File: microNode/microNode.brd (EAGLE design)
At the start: 65 x 30 mm, 29 parts, among them U1 ATSAMD21G18A-AU, U2 TPL5111, U3 RFM95W-868S2, U4 MIC5504-3.3YM5-T5, U6 CLX6E-FKC-CH1M1D1BB7C3D3, U7 SIP32431DR3, U8 PCF2123, Y1 ABS07, Y2 ABS07

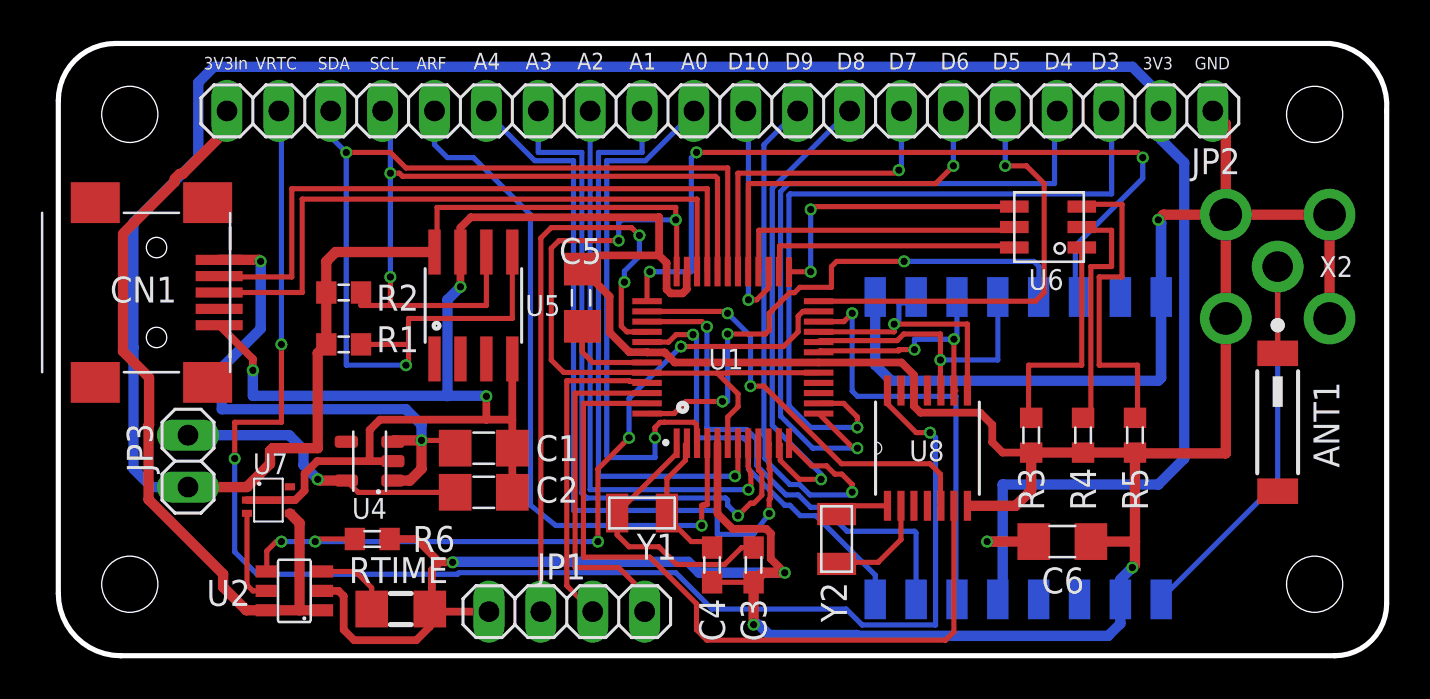
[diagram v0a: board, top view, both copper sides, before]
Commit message: Display connector/ RST button/ side led
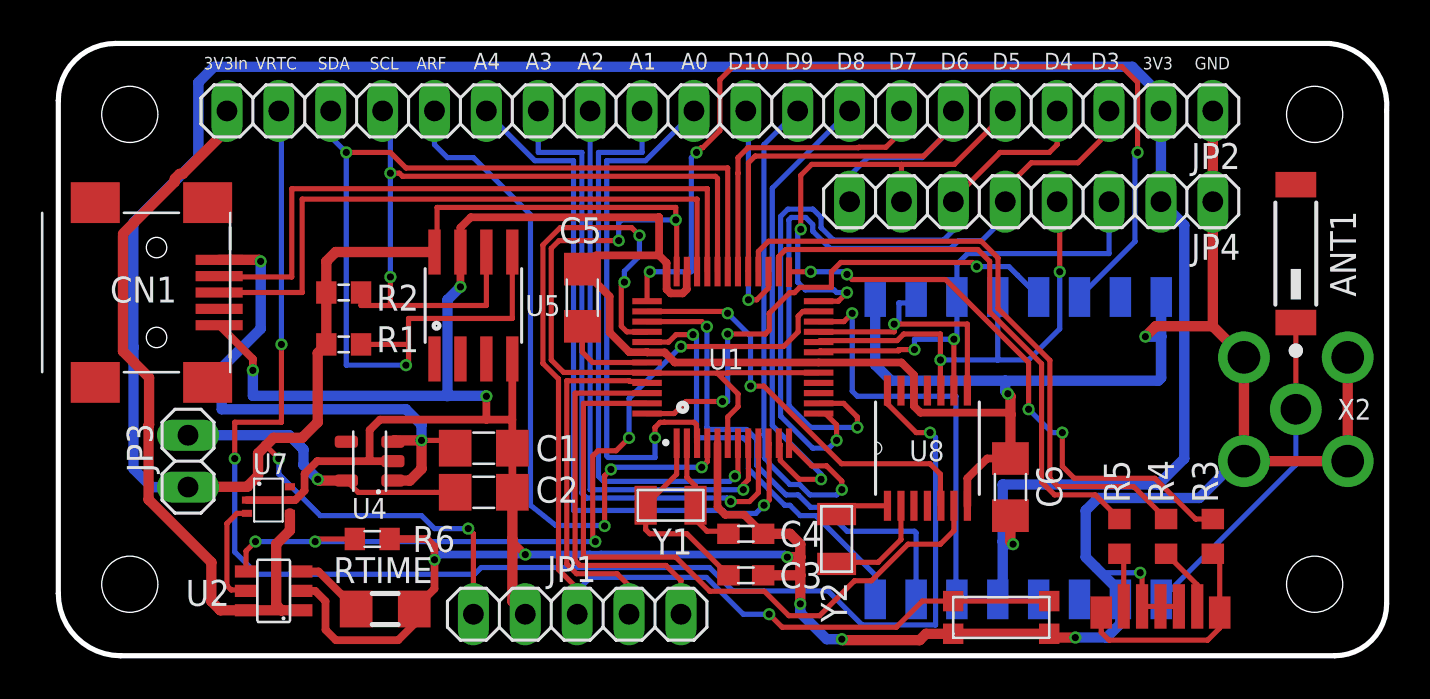
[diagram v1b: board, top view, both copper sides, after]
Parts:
- removed U6: CLX6E-FKC-CH1M1D1BB7C3D3, CLX6E-FKC:CLX6E-FKC-CH1M1D1BB7C3D3
- added JP4: (no value), pinhead:1X08
- added U$1: MSL0104RGB, MSL0104RGB:MSL0104RGB
- added U$2: KMR731NG, button:KMR731NG
- JP1: device pinhead:1X04 -> pinhead:1X05
- moved R3 10.2 mm to (104.8, 41.4)
- moved ANT1 8.30 mm to (108.8, 55.2), turned to 90 degrees
- moved X2 7.04 mm to (108.8, 47.6)
- moved R4 6.41 mm to (102.5, 41.4)
- moved R5 5.01 mm to (100.2, 41.4)
- moved C6 3.68 mm to (94.9, 43.8), turned to 90 degrees
- moved C4 2.25 mm to (81.9, 41.5), turned to 0 degrees
- moved Y1 1.45 mm to (78.2, 42.9)
- moved U2 1.02 mm to (58.8, 38.7)
- moved RTIME 0.76 mm to (64.3, 37.8)
- moved C3 0.64 mm to (81.9, 39.5), turned to 0 degrees
- moved JP1 0.52 mm to (73.7, 37.6)
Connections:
- removed net N$10: R5.2, U6.P$3
- removed net N$7: R3.2, U6.P$1
- removed net N$9: R4.2, U6.P$2
- new net N$12: R3.1, U$1.P$1, U$1.P$7
- new net N$13: R4.1, U$1.P$2
- new net N$14: R5.1, U$1.P$6
- net 3V3: now also JP1.1, JP4.2
- net D11: now also R3.2; no longer U6.P$4
- net D12: now also R4.2; no longer U6.P$5
- net D13: now also R5.2; no longer U6.P$6
- net D3: now also JP4.5
- net D4: now also JP4.6
- net D5: now also JP4.7
- net D6: now also JP4.8
- net GND: now also JP1.2, JP4.1, U$1.P$3, U$1.P$4, U$1.P$5, U$2.P$3, U$2.P$4; no longer JP1.1, R3.1, R4.1, R5.1
- net MOSI: now also JP4.3
- net RST: now also JP1.3, U$2.P$1, U$2.P$2; no longer JP1.2
- net SCK: now also JP4.4
- net SWCLK: now also JP1.4; no longer JP1.3
- net SWDIO: now also JP1.5; no longer JP1.4
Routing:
- net RST: track 29.7 -> 56.3 mm, vias 2 -> 3
- net GND: track 278.7 -> 252.5 mm, vias 8 -> 12
- net D12: track 14.7 -> 31.6 mm
- net N$10: track 15.7 -> 0.00 mm
- net D13: track 12.9 -> 27.9 mm
- net D11: track 14.2 -> 28.1 mm, vias 2 -> 4
- net N$9: track 12.2 -> 0.00 mm
- net MOSI: track 12.5 -> 23.8 mm
- net N$7: track 11.1 -> 0.00 mm
- net N$12: track 0.00 -> 11.0 mm
- net 3V3: track 181.7 -> 192.0 mm, vias 3 -> 5
- net SCK: track 14.8 -> 24.8 mm, vias 1 -> 2
- net D6: track 17.4 -> 25.0 mm, vias 1 -> 0
- net ANT: track 22.9 -> 16.3 mm
- net RAD_RESET: track 39.7 -> 46.3 mm
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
